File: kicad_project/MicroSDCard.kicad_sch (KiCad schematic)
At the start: 18 parts, among them J8 DM3AT, U14 74AHC1G04, U21 SN74AXC4T774, U22 AP22913W6-7

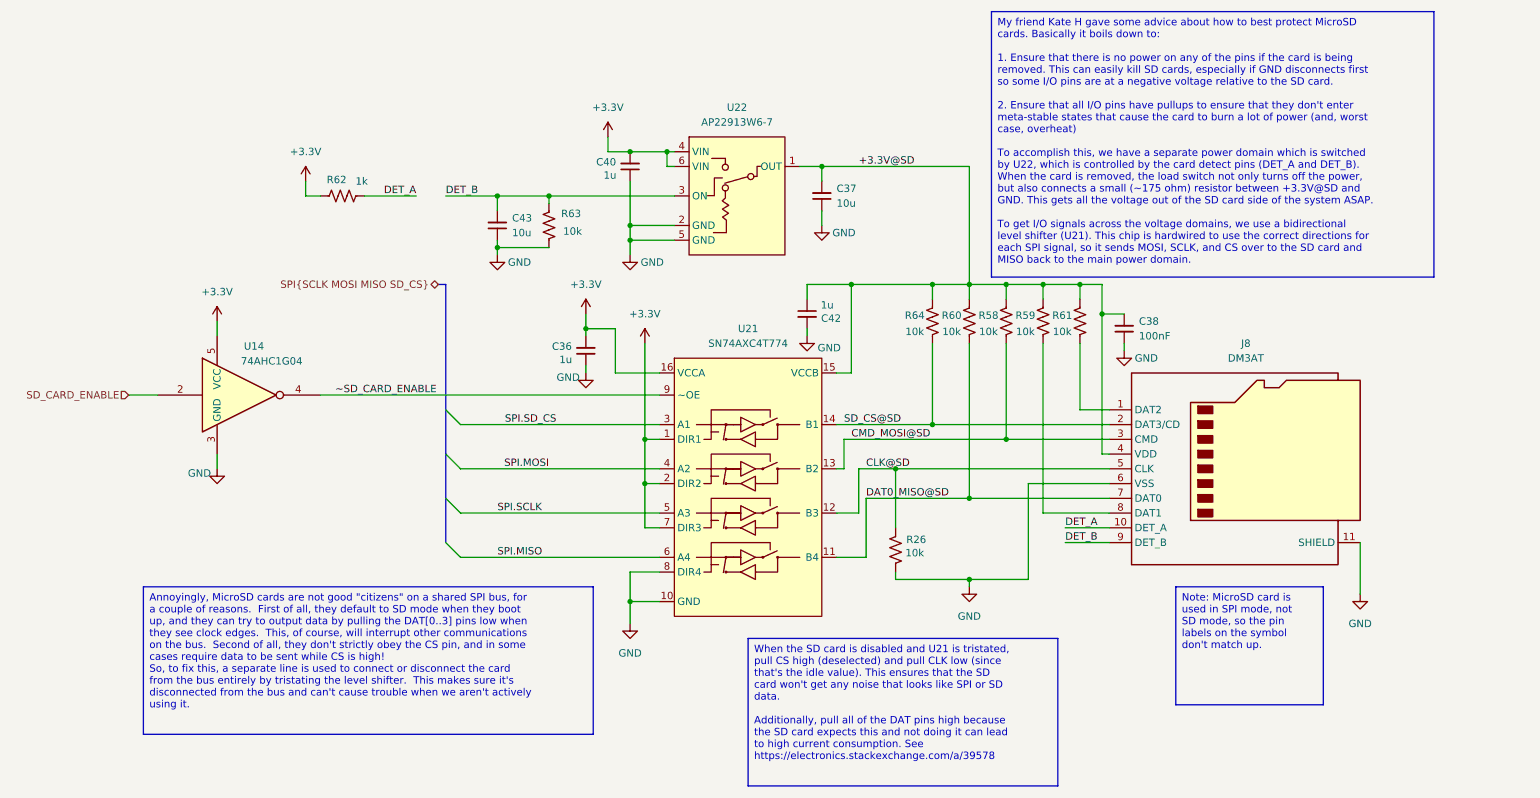
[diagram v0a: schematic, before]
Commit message: Switch out multiplexer, start switch FX2LP out for RP2040
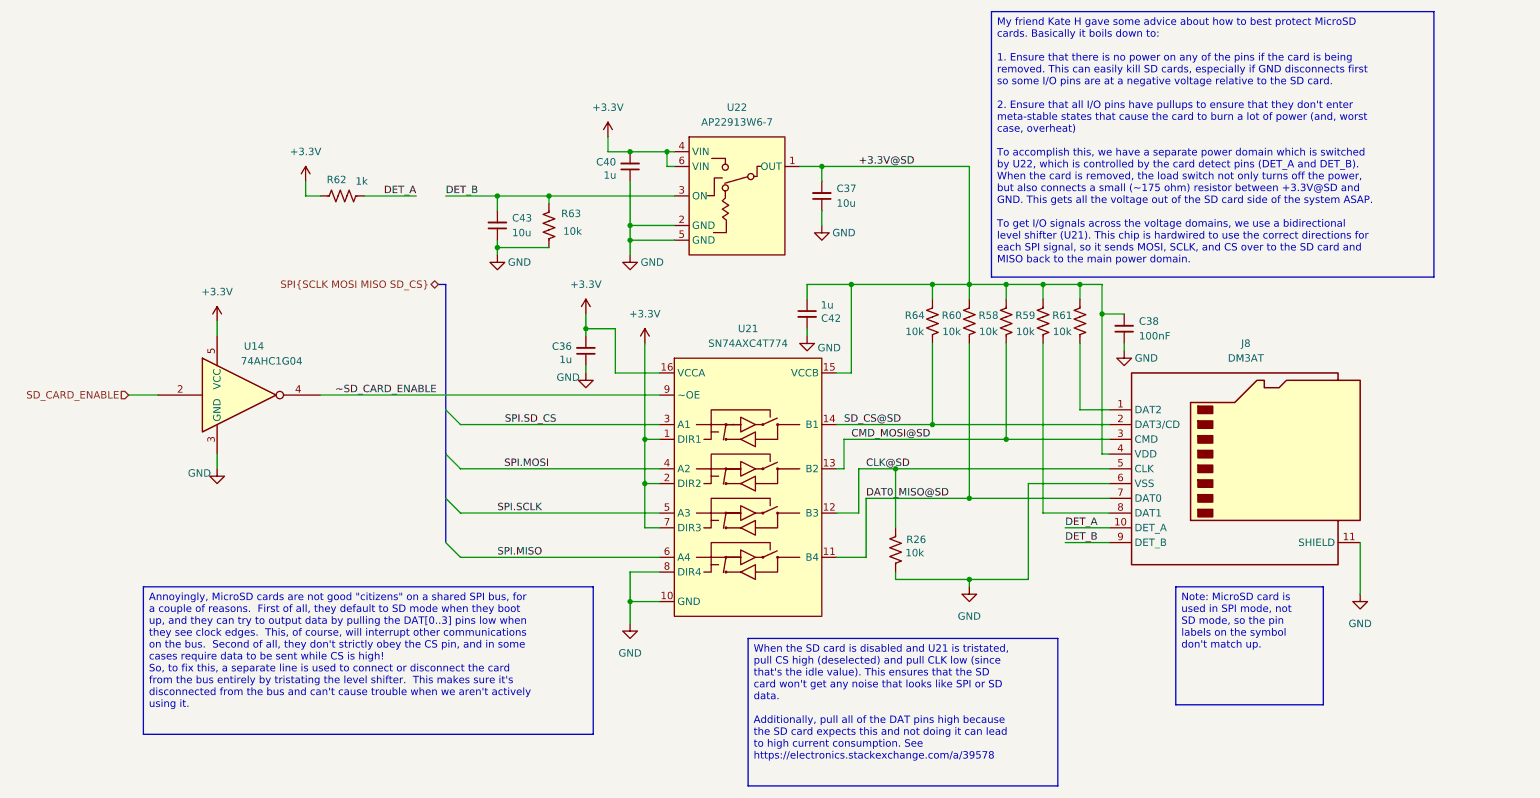
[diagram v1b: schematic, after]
